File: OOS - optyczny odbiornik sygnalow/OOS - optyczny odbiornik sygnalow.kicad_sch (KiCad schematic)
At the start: 52 parts, among them J1 Conn_01x02_Socket, J2 Conn_01x02_Socket, J3 Conn_01x02_Socket, J4 Conn_01x02_Socket, J5 Conn_Coaxial, U1 OPA300AIDBVR, U2 OPA300AIDBVR

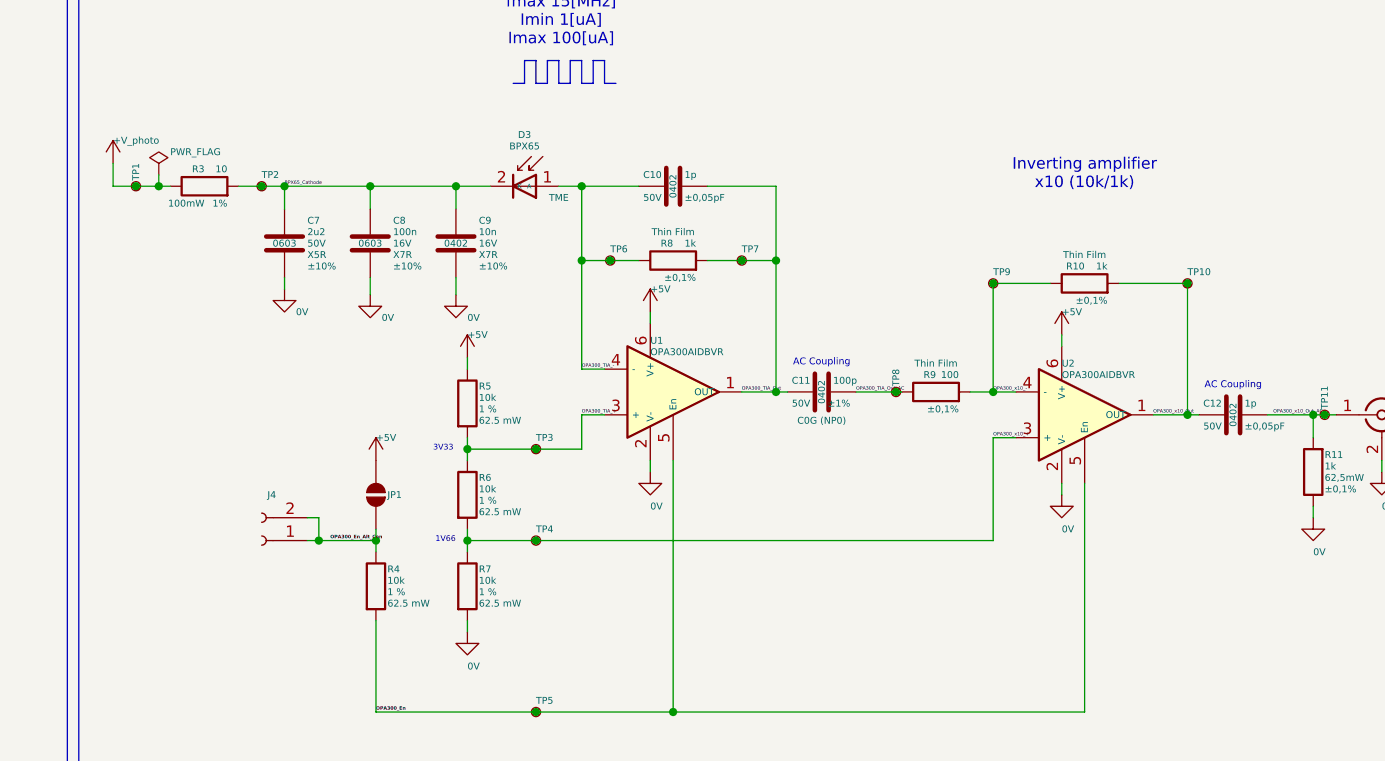
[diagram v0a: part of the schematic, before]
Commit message: Dodanie wielkosci obudow do reszty kompoenntow, poprawienie polozenia parametrow dla komponentow
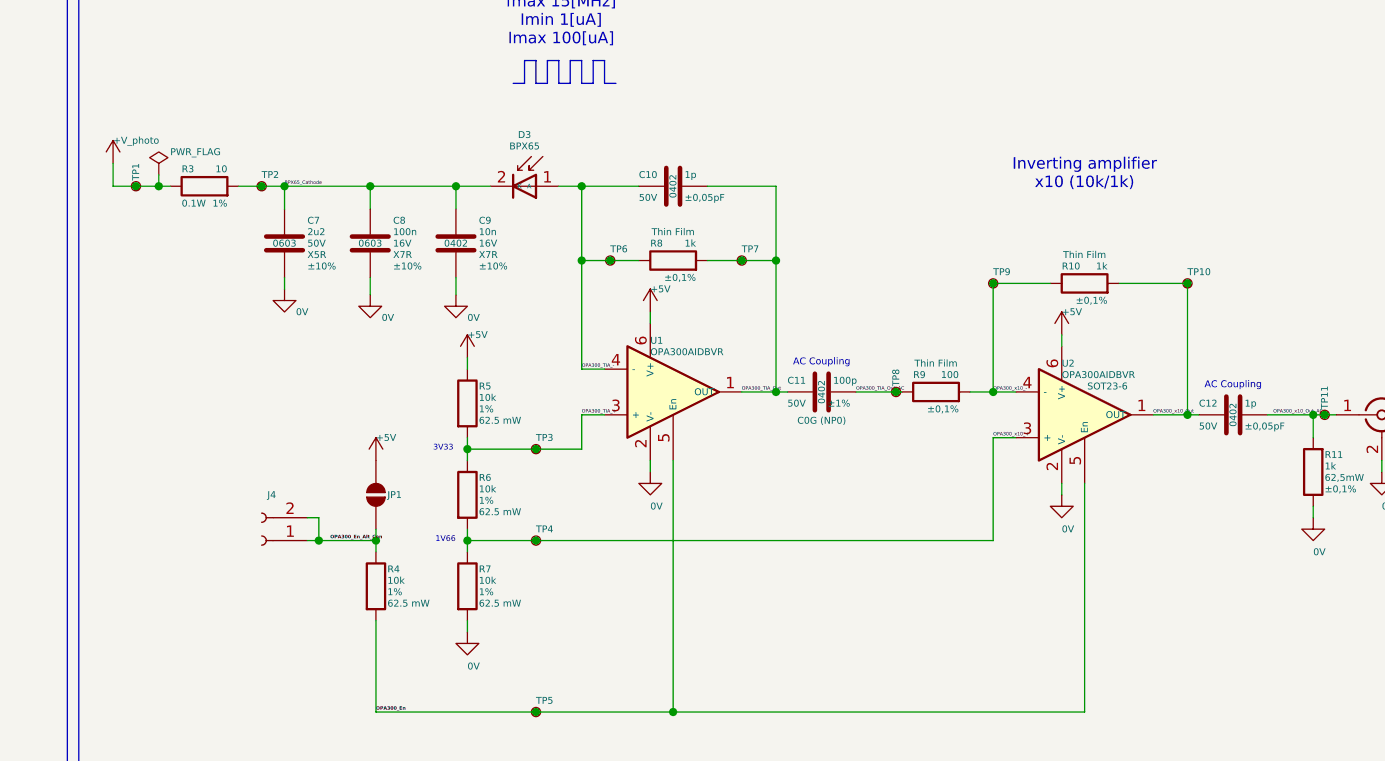
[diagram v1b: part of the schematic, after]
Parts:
- D1, D2, R1, R2: Package (none) -> 0603
- D3: Package (none) -> TO-18-2
- R10, R11, R8: Package (none) -> 0402
- R3: Package (none) -> 0603; Power Rating 100mW -> 0.1W
- R4, R5, R6, R7: Package (none) -> 0402; Tolerance 1 % -> 1%
- U1, U2: Package (none) -> SOT23-6
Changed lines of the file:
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@@
 			)
 		)
-		(property "Tolerance" "1 %"
+		(property "Tolerance" "1%"
 			(at 156.21 121.92 0)
 			(effects
@@
 			)
 		)
+		(property "Package" "0402"
+			(at 154.94 121.285 0)
+			(effects
+				(font
+					(size 0.762 0.762)
+				)
+				(hide yes)
+			)
+		)
 		(pin "1"
 		)
@@
 		(dnp no)
 		(property "Reference" "C10"
-			(at 186.69 75.565 90)
+			(at 184.15 75.565 90)
 			(effects
 				(font
 					(size 0.762 0.762)
 				)
-				(justify left)
+				(justify right)
 			)
 		)
@@
 		)
 		(property "Voltage Rating" "50V"
-			(at 186.69 78.105 90)
+			(at 184.15 78.105 90)
 			(effects
 				(font
 					(size 0.762 0.762)
 				)
-				(justify left)
+				(justify right)
 			)
 		)
@@
 			)
 		)
+		(property "Package" "0402"
+			(at 259.08 108.585 0)
+			(effects
+				(font
+					(size 0.762 0.762)
+				)
+				(hide yes)
+			)
+		)
 		(pin "2"
 		)
@@
 			)
 		)
-		(property "Tolerance" "1 %"
+		(property "Tolerance" "1%"
 			(at 166.37 111.76 0)
 			(effects
@@
 			)
 		)
+		(property "Package" "0402"
+			(at 165.1 111.125 0)
+			(effects
+				(font
+					(size 0.762 0.762)
+				)
+				(hide yes)
+			)
+		)
 		(pin "1"
 		)
@@
 		(dnp no)
 		(property "Reference" "R9"
-			(at 217.17 97.79 90)
+			(at 214.63 97.79 90)
 			(effects
 				(font
 					(size 0.762 0.762)
 				)
-				(justify left)
+				(justify right)
 			)
 		)
@@
 			)
 		)
+		(property "Package" "0603"
+			(at 88.9 104.775 0)
+			(effects
+				(font
+					(size 0.762 0.762)
+				)
+				(hide yes)
+			)
+		)
 		(pin "1"
 		)
@@
 			)
 		)
+		(property "Package" "SOT23-6"
+			(at 236.22 99.06 0)
+			(effects
+				(font
+					(size 0.762 0.762)
+				)
+			)
+		)
 		(pin "3"
 		)
@@
 		(dnp no)
 		(property "Reference" "R3"
-			(at 135.89 74.93 90)
+			(at 133.35 74.93 90)
 			(effects
 				(font
 					(size 0.762 0.762)
 				)
-				(justify left)
+				(justify right)
 			)
 		)
@@
 			)
 		)
-		(property "Power Rating" "100mW"
-			(at 135.89 78.74 90)
+		(property "Power Rating" "0.1W"
+			(at 133.35 78.74 90)
 			(effects
 				(font
 					(size 0.762 0.762)
 				)
-				(justify left)
+				(justify right)
 			)
 		)
@@
 			)
 		)
+		(property "Package" "0603"
+			(at 135.89 76.835 90)
+			(effects
+				(font
+					(size 0.762 0.762)
+				)
+				(hide yes)
+			)
+		)
 		(pin "2"
 		)
@@
 					(size 0.762 0.762)
 				)
+				(hide yes)
+			)
+		)
+		(property "Package" "TO-18-2"
+			(at 175.514 79.248 0)
+			(effects
+				(font
+					(size 0.762 0.762)
+				)
+				(hide yes)
 			)
 		)
@@
 			)
 		)
+		(property "Package" "0603"
+			(at 88.9 113.665 90)
+			(effects
+				(font
+					(size 0.762 0.762)
+				)
+				(hide yes)
+			)
+		)
 		(pin "2"
 		)
@@
 			)
 		)
+		(property "Package" "0603"
+			(at 76.2 104.775 0)
+			(effects
+				(font
+					(size 0.762 0.762)
+				)
+				(hide yes)
+			)
+		)
 		(pin "1"
 		)
@@
 			)
 		)
-		(property "Tolerance" "1 %"
+		(property "Tolerance" "1%"
 			(at 166.37 101.6 0)
 			(effects
@@
 			)
 		)
+		(property "Package" "0402"
+			(at 165.1 100.965 0)
+			(effects
+				(font
+					(size 0.762 0.762)
+				)
+				(hide yes)
+			)
+		)
 		(pin "1"
 		)
@@
 			)
 		)
-		(property "Tolerance" "1 %"
+		(property "Tolerance" "1%"
 			(at 166.37 121.92 0)
 			(effects
@@
 			)
 		)
+		(property "Package" "0402"
+			(at 165.1 121.285 0)
+			(effects
+				(font
+					(size 0.762 0.762)
+				)
+				(hide yes)
+			)
+		)
 		(pin "1"
 		)
@@
 			)
 		)
+		(property "Package" "SOT23-6"
+			(at 180.34 92.075 0)
+			(effects
+				(font
+					(size 0.762 0.762)
+				)
+				(hide yes)
+			)
+		)
 		(pin "3"
 		)
@@
 		(dnp no)
 		(property "Reference" "R8"
-			(at 187.96 83.185 90)
+			(at 185.42 83.185 90)
 			(effects
 				(font
 					(size 0.762 0.762)
 				)
-				(justify left)
+				(justify right)
 			)
 		)
@@
 			)
 		)
+		(property "Package" "0402"
+			(at 187.96 85.09 90)
+			(effects
+				(font
+					(size 0.762 0.762)
+				)
+				(hide yes)
+			)
+		)
 		(pin "2"
 		)
@@
 			)
 		)
+		(property "Package" "0603"
+			(at 76.2 113.665 90)
+			(effects
+				(font
+					(size 0.762 0.762)
+				)
+				(hide yes)
+			)
+		)
 		(pin "2"
 		)
@@
 		(dnp no)
 		(property "Reference" "C11"
-			(at 203.2 98.425 90)
+			(at 200.66 98.425 90)
 			(effects
 				(font
 					(size 0.762 0.762)
 				)
-				(justify left)
+				(justify right)
 			)
 		)
@@
 		)
 		(property "Voltage Rating" "50V"
-			(at 203.2 100.965 90)
+			(at 200.66 100.965 90)
 			(effects
 				(font
 					(size 0.762 0.762)
 				)
-				(justify left)
+				(justify right)
 			)
 		)
@@
 		(dnp no)
 		(property "Reference" "C12"
-			(at 248.92 100.965 90)
+			(at 246.38 100.965 90)
 			(effects
 				(font
 					(size 0.762 0.762)
 				)
-				(justify left)
+				(justify right)
 			)
 		)
@@
 		)
 		(property "Voltage Rating" "50V"
-			(at 248.92 103.505 90)
+			(at 246.38 103.505 90)
 			(effects
 				(font
 					(size 0.762 0.762)
 				)
-				(justify left)
+				(justify right)
 			)
 		)
@@
 		(dnp no)
 		(property "Reference" "R10"
-			(at 233.68 85.725 90)
+			(at 231.14 85.725 90)
 			(effects
 				(font
 					(size 0.762 0.762)
 				)
-				(justify left)
+				(justify right)
 			)
 		)
@@
 			(effects
 				(font
+					(size 0.762 0.762)
+				)
+				(hide yes)
+			)
+		)
+		(property "Package" "0402"
+			(at 233.68 87.63 90)
+			(effects
+				(font

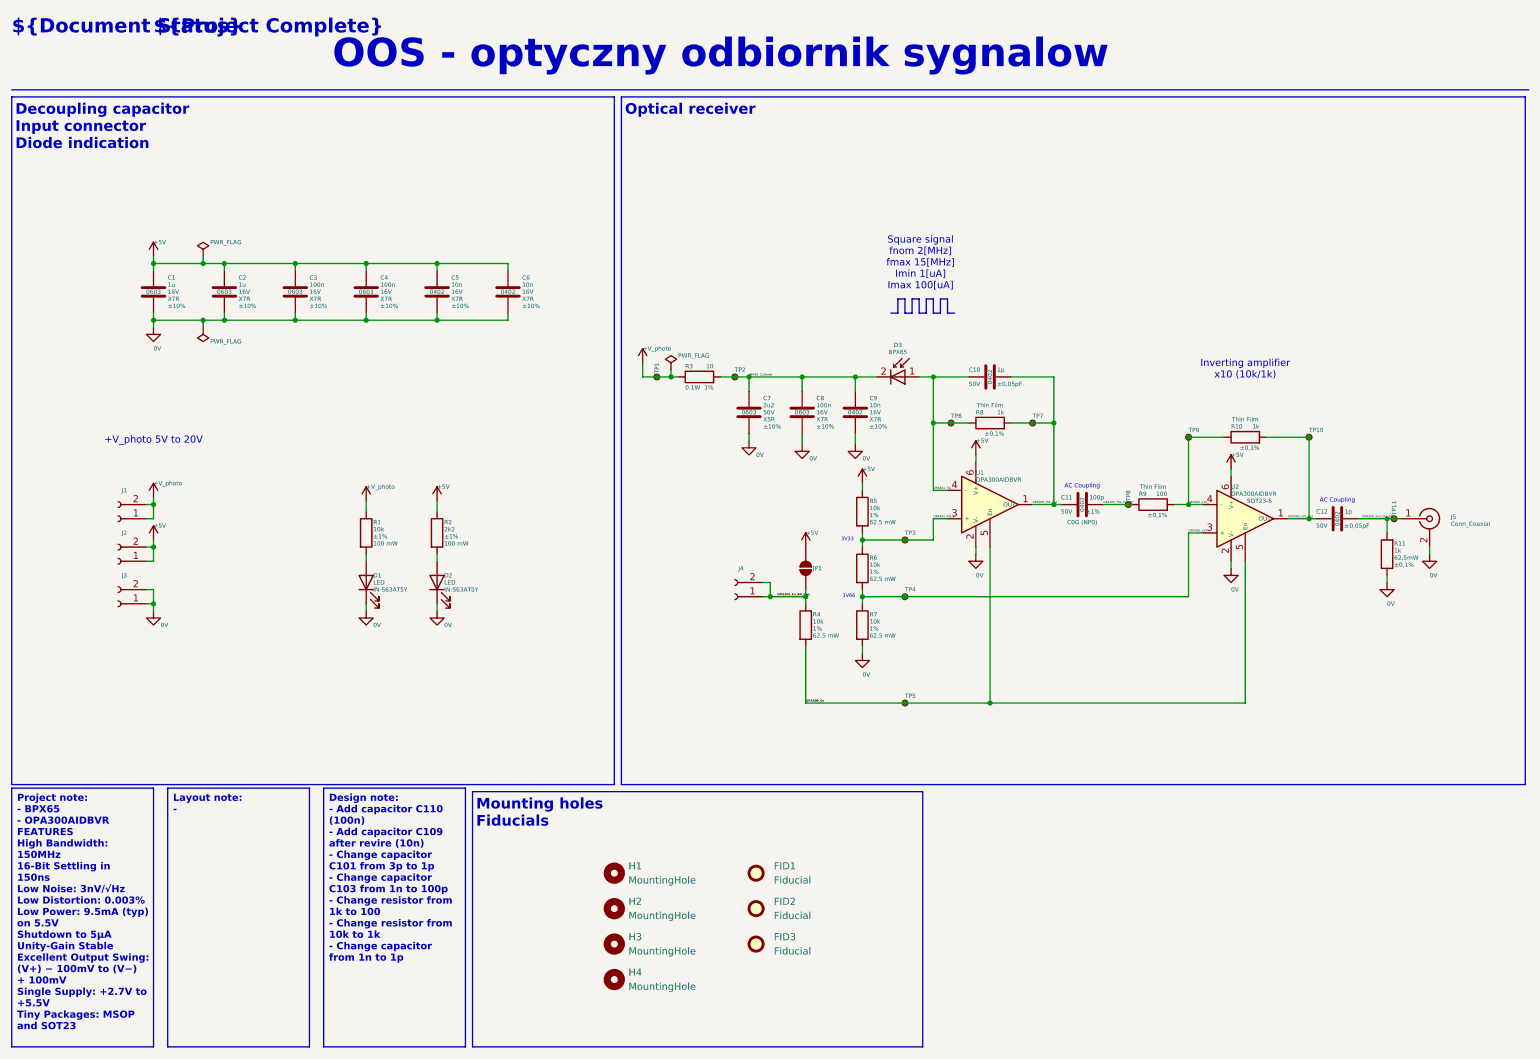
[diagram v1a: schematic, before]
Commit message: Rozdzielenie projektu na strony, analogowa, ladowanie, usb, boost
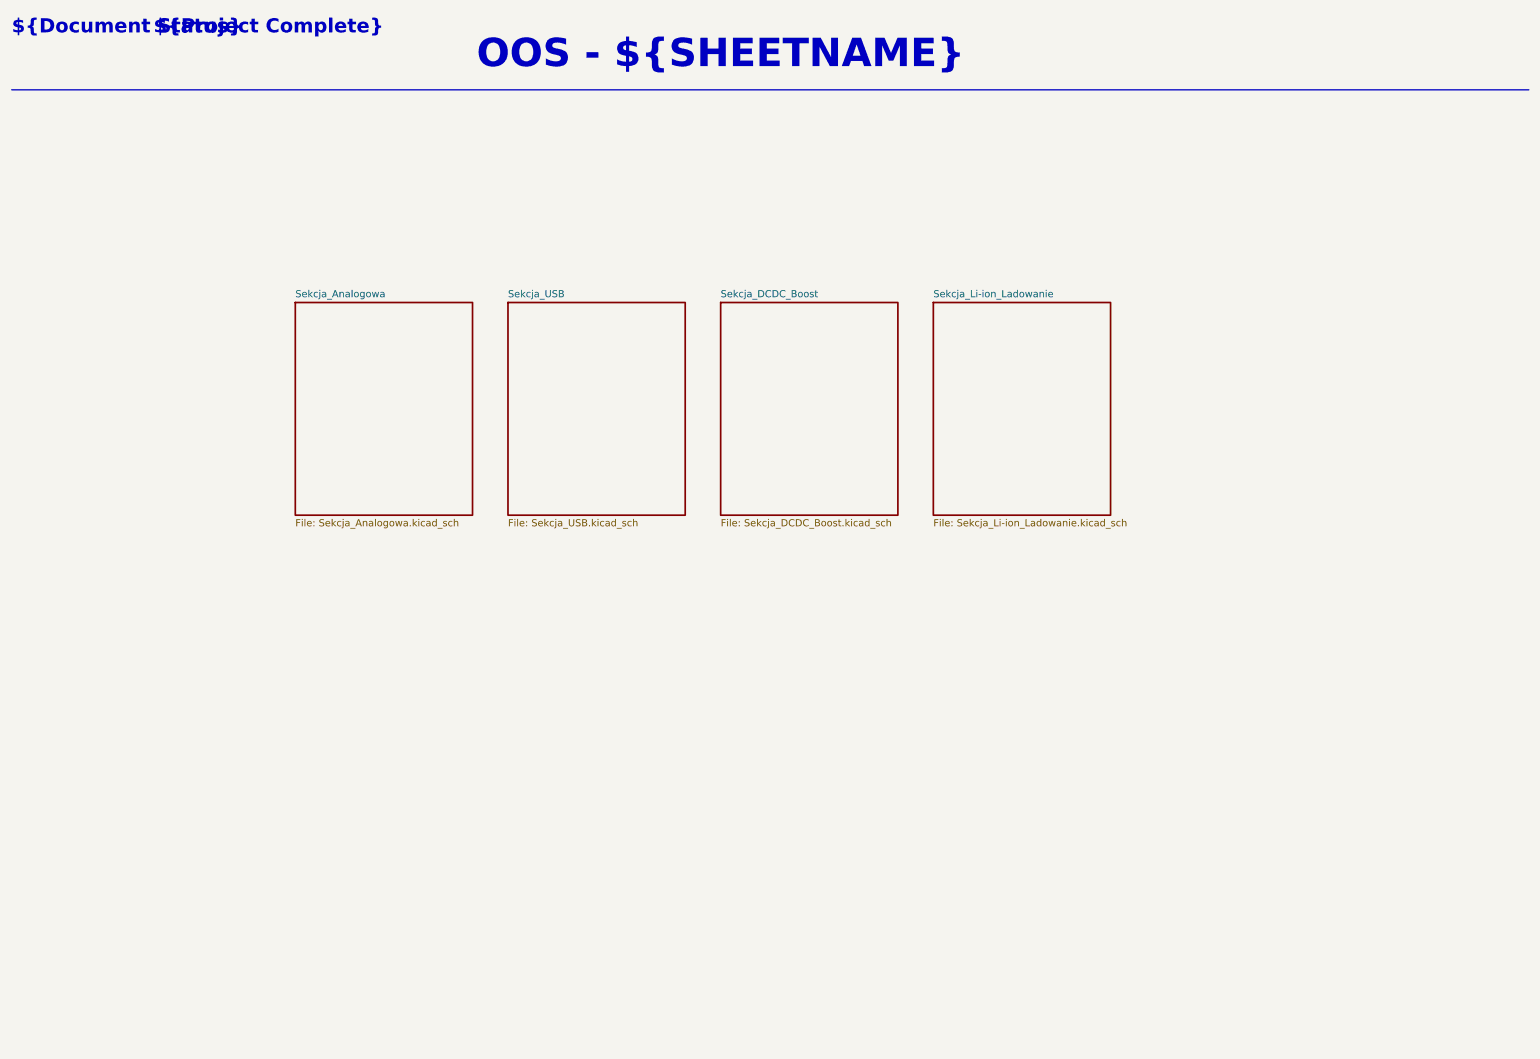
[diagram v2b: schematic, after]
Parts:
- removed C1, C2: 1u, Capacitor_SMD:C_0603_1608Metric, symbol Device:C
- removed C10, C12: 1p, Capacitor_SMD:C_0402_1005Metric, symbol Device:C
- removed C11: 100p, Capacitor_SMD:C_0402_1005Metric, symbol Device:C
- removed C3, C4, C8: 100n, Capacitor_SMD:C_0603_1608Metric, symbol Device:C
- removed C5, C6, C9: 10n, Capacitor_SMD:C_0402_1005Metric, symbol Device:C
- removed C7: 2u2, Capacitor_SMD:C_0603_1608Metric, symbol Device:C
- removed D1, D2: LED, Diode_SMD:D_0603_1608Metric, symbol Device:LED
- removed D3: BPX65, Package_TO_SOT_THT:TO-18-2_Lens, symbol QP Biblioteka:BPX65
- removed FID1, FID2, FID3: Fiducial, Fiducial:Fiducial_1.5mm_Mask3mm, symbol Mechanical:Fiducial
- removed H1, H2, H3, H4: MountingHole, MountingHole:MountingHole_3.2mm_M3, symbol Mechanical:MountingHole
- removed J1, J2, J3, J4: Conn_01x02_Socket, Connector_PinHeader_2.54mm:PinHeader_1x02_P2.54mm_Vertical, symbol Connector:Conn_01x02_Socket
- removed J5: Conn_Coaxial, Connector_Coaxial:BNC_Amphenol_B6252HB-NPP3G-50_Horizontal, symbol Connector:Conn_Coaxial
- removed JP1: SolderJumper_2_Open, Jumper:SolderJumper-2_P1.3mm_Bridged_RoundedPad1.0x1.5mm, symbol Jumper:SolderJumper_2_Open
- removed R1: 10k, Resistor_SMD:R_0603_1608Metric, symbol Device:R
- removed R10, R11, R8: 1k, Resistor_SMD:R_0402_1005Metric, symbol Device:R
- removed R2: 2k2, Resistor_SMD:R_0603_1608Metric, symbol Device:R
- removed R3: 10, Resistor_SMD:R_0603_1608Metric, symbol Device:R
- removed R4, R5, R6, R7: 10k, Resistor_SMD:R_0402_1005Metric, symbol Device:R
- removed R9: 100, Resistor_SMD:R_0402_1005Metric, symbol Device:R
- removed TP1, TP10, TP11, TP2, TP3, TP4, TP5, TP6, TP7, TP8, TP9: TestPoint_Small, TestPoint:TestPoint_Pad_D1.0mm, symbol Connector:TestPoint_Small
- removed U1, U2: OPA300AIDBVR, Package_TO_SOT_SMD:SOT-23-6_Handsoldering, symbol QP Biblioteka:OPA300AIDBVR
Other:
- added sheet Sekcja_Analogowa (Sekcja_Analogowa.kicad_sch)
- added sheet Sekcja_DCDC_Boost (Sekcja_DCDC_Boost.kicad_sch)
- added sheet Sekcja_Li-ion_Ladowanie (Sekcja_Li-ion_Ladowanie.kicad_sch)
- added sheet Sekcja_USB (Sekcja_USB.kicad_sch)
- note added: "OOS - ${SHEETNAME}"
- note removed: "+V_photo 5V to 20V"
- note removed: "1V66"
- note removed: "3V33"
- note removed: "AC Coupling"
- note removed: "Decoupling capacitor Input connector Diode indication"
- note removed: "Inverting amplifier x10 (10k/1k)"
- note removed: "Mounting holes Fiducials"
- note removed: "OOS - optyczny odbiornik sygnalow"
- note removed: "Optical receiver"
- note removed: "Square signal fnom 2[MHz] fmax 15[MHz] Imin 1[uA] Imax 100[uA]"
